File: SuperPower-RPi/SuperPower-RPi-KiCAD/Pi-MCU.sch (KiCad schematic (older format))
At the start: 30 parts, among them J5 Conn_01x06, J7 Conn_01x03, J8 Conn_01x10, J9 Conn_01x02, SW1 Tact, U3 STM32F412RETx, U4 ATtiny85-20SU, U5 ME6210A33M3G

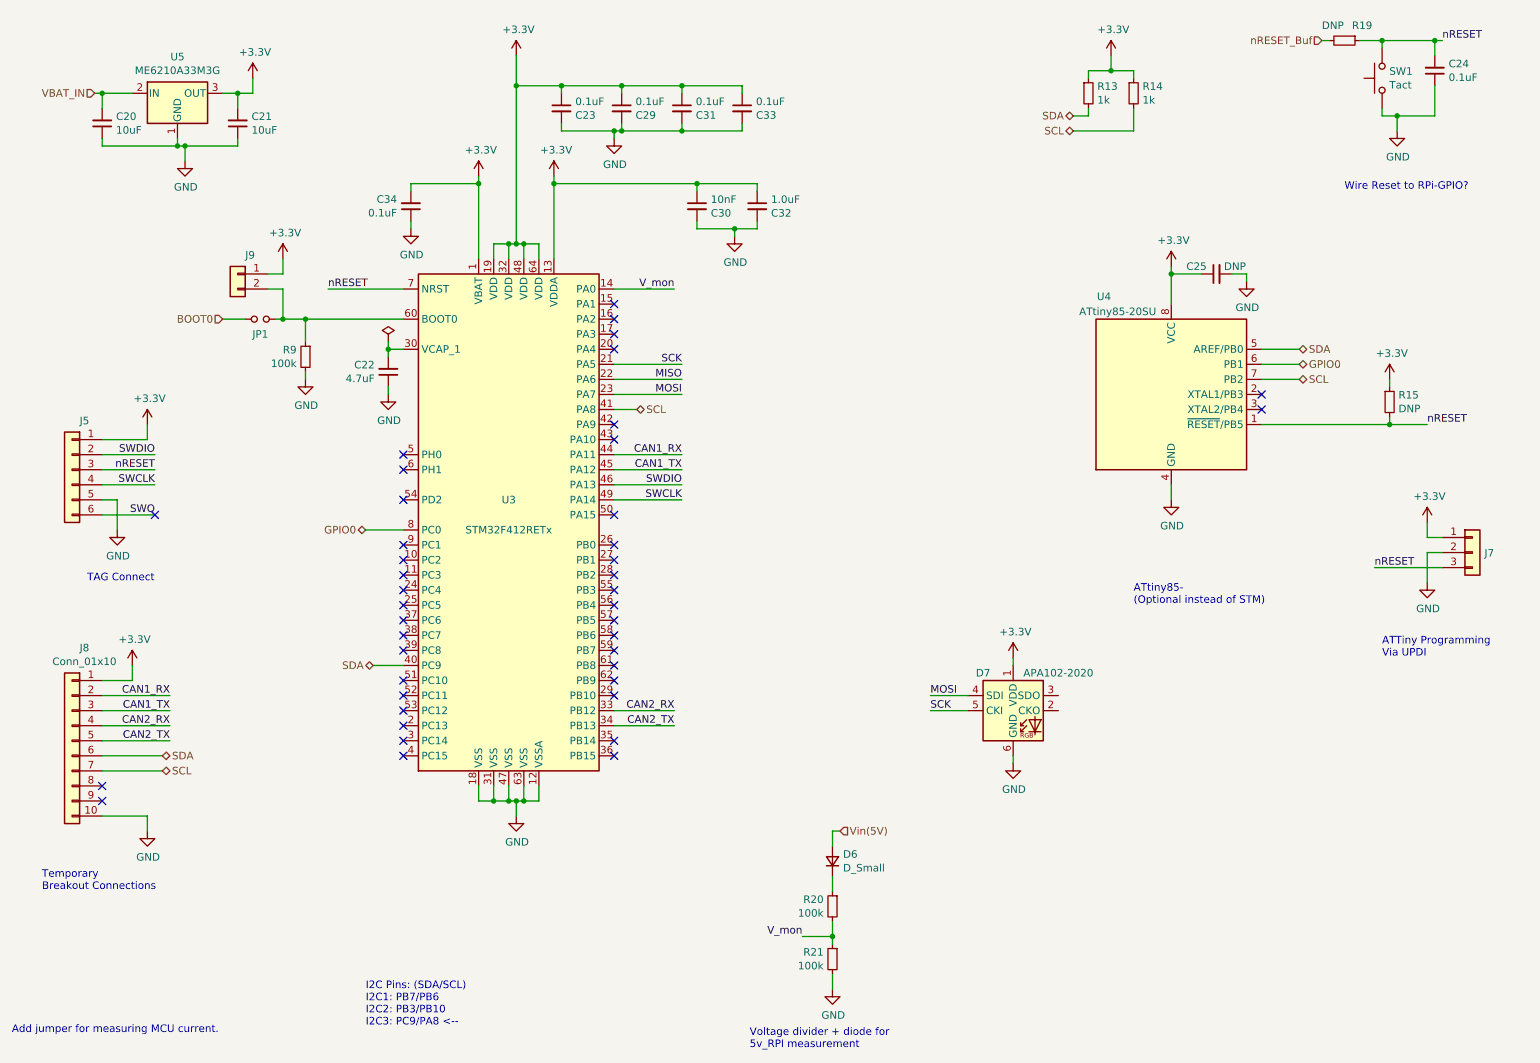
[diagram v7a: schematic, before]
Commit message: Added TODO notes from today's meeting and added some items on MCU sheet.
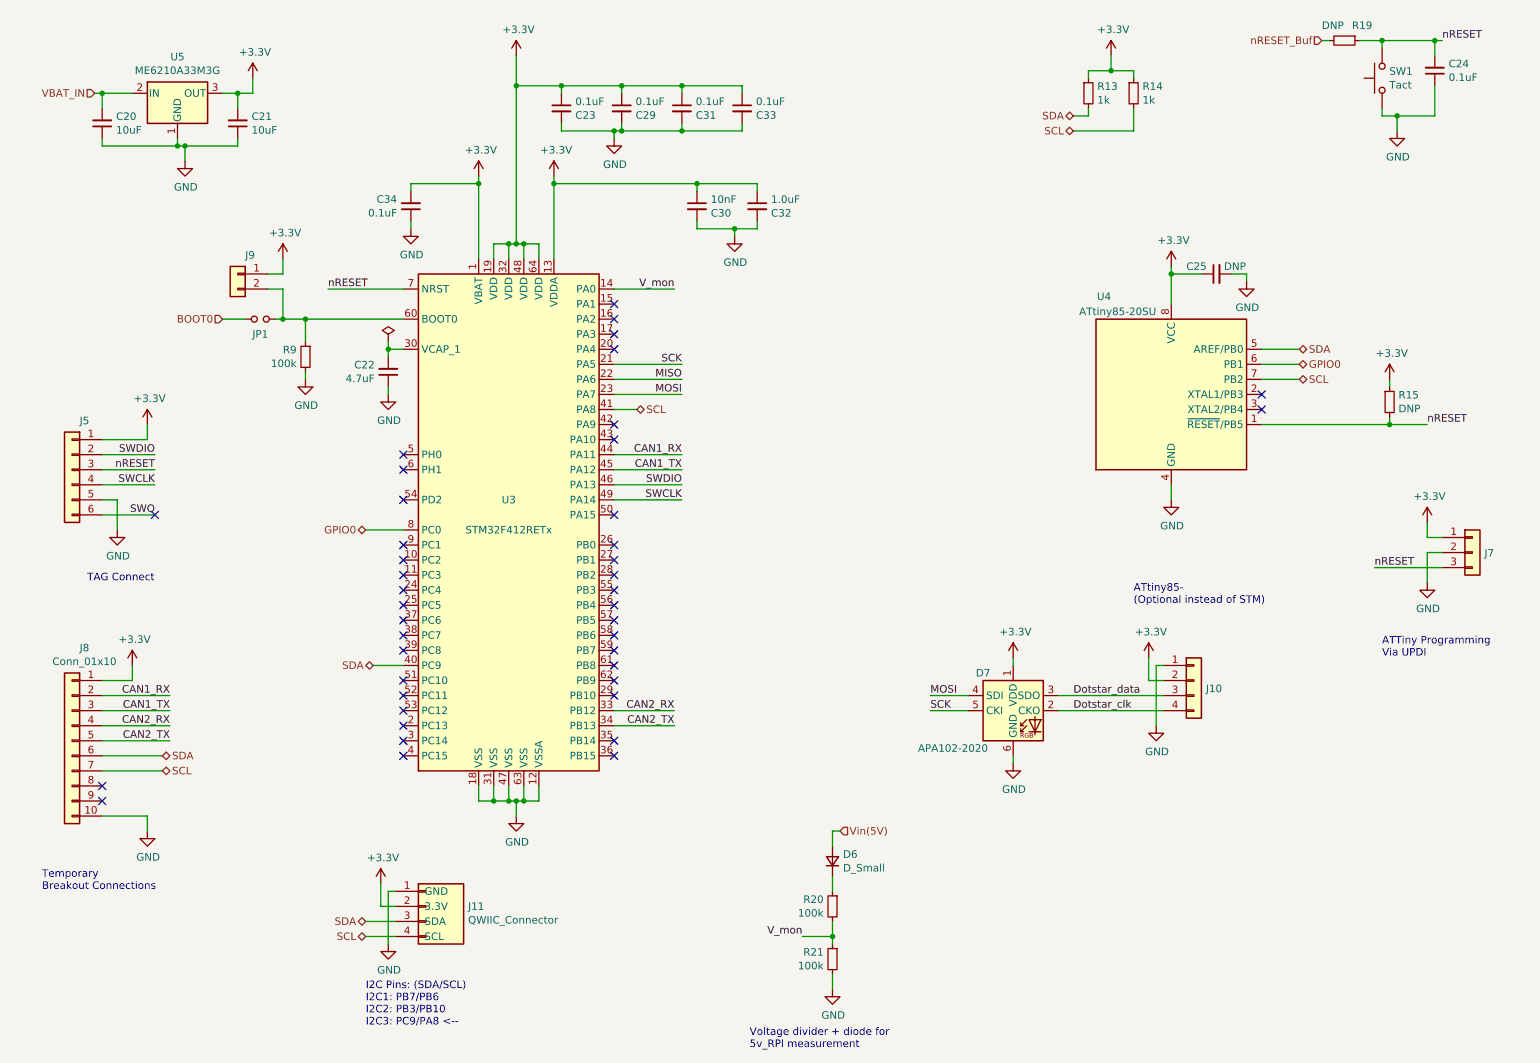
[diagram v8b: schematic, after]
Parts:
- added J10: Conn_01x04, Connector_PinHeader_2.54mm:PinHeader_1x04_P2.54mm_Vertical, symbol Connector_Generic:Conn_01x04
- added J11: QWIIC_Connector, Connector_JST:JST_SH_SM04B-SRSS-TB_1x04-1MP_P1.00mm_Horizontal, symbol !Seth_Components:QWIIC_Connector
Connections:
- net +3V3: now also J10.2 (Pin_2), J11.2 (3.3V)
- net GND: now also J10.1 (Pin_1), J11.1 (GND)
- net SCL: now also J11.4 (SCL)
- net SDA: now also J11.3 (SDA)
- net Dotstar_clk: now reaches D7.2 (CKO)
- net Dotstar_clk: now also J10.4 (Pin_4)
- net Dotstar_data: now reaches D7.3 (SDO)
- net Dotstar_data: now also J10.3 (Pin_3)
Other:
- note removed: "Add jumper for measuring MCU current."
- note removed: "Wire Reset to RPi-GPIO?"
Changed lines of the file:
@@
 $Descr A4 11693 8268
 encoding utf-8
-Sheet 8 8
+Sheet 7 8
 Title ""
 Date ""
@@
 Text HLabel 3150 4150 0    50   BiDi ~ 0
 GPIO0
-Text Notes 800  7500 0    50   ~ 0
-Add jumper for measuring MCU current.
 Text HLabel 7850 1400 0    50   BiDi ~ 0
 SDA
@@
 Wire Wire Line
 	2600 2450 2600 2350
-Text Notes 9650 1900 0    50   ~ 0
-Wire Reset to RPi-GPIO?
 $Comp
 L Device:R_Small R19
@@
 P 7450 5350
 F 0 "D7" H 7250 5600 50  0000 C CNN
-F 1 "APA102-2020" H 7750 5600 50  0000 C CNN
+F 1 "APA102-2020" H 7050 5100 50  0000 C CNN
 F 2 "LED_SMD:LED-APA102-2020" H 7500 5050 50  0001 L TNN
 F 3 "http://www.led-color.com/upload/201604/APA102-2020%20SMD%20LED.pdf" H 7550 4975 50  0001 L TNN
@@
 Wire Wire Line
 	7450 5000 7450 5050
+$Comp
+L Connector_Generic:Conn_01x04 J10
+U 1 1 5FBFB7CE
+P 8650 5150
+F 0 "J10" H 8730 5096 50  0000 L CNN
+F 1 "Conn_01x04" H 8730 5051 50  0001 L CNN
+F 2 "Connector_PinHeader_2.54mm:PinHeader_1x04_P2.54mm_Vertical" H 8650 5150 50  0001 C CNN
+F 3 "~" H 8650 5150 50  0001 C CNN
+	1    8650 5150
+	1    0    0    -1
+$EndComp
+Wire Wire Line
+	7750 5250 8450 5250
+Wire Wire Line
+	8450 5350 7750 5350
+$Comp
+L power:+3.3V #PWR042
+U 1 1 5FC175FC
+P 8350 5000
+F 0 "#PWR042" H 8350 4850 50  0001 C CNN
+F 1 "+3.3V" H 8365 5173 50  0000 C CNN
+F 2 "" H 8350 5000 50  0001 C CNN
+F 3 "" H 8350 5000 50  0001 C CNN
+	1    8350 5000
+	1    0    0    -1
+$EndComp
+Wire Wire Line
+	8450 5150 8350 5150
+Wire Wire Line
+	8350 5150 8350 5000
+$Comp
+L power:GND #PWR043
+U 1 1 5FC1F7CE
+P 8400 5450
+F 0 "#PWR043" H 8400 5200 50  0001 C CNN
+F 1 "GND" H 8405 5277 50  0000 C CNN
+F 2 "" H 8400 5450 50  0001 C CNN
+F 3 "" H 8400 5450 50  0001 C CNN
+	1    8400 5450
+	1    0    0    -1
+$EndComp
+Wire Wire Line
+	8400 5450 8400 5050
+Wire Wire Line
+	8400 5050 8450 5050
+$Comp
+L !Seth_Components:QWIIC_Connector J11
+U 1 1 5FC07762
+P 3550 6650
+F 0 "J11" H 3830 6650 50  0000 L CNN
+F 1 "QWIIC_Connector" H 3830 6559 50  0000 L CNN
+F 2 "Connector_JST:JST_SH_SM04B-SRSS-TB_1x04-1MP_P1.00mm_Horizontal" H 5200 6750 50  0001 C CNN
+F 3 "http://www.jst-mfg.com/product/pdf/eng/eSH.pdf" H 3550 6650 50  0001 C CNN
+F 4 "JST" H 3900 6600 50  0001 C CNN "Mfg"
+F 5 "SM04B-SRSS-TB(LF)(SN)" H 4300 6850 50  0001 C CNN "Mfg PN"
+F 6 "455-1804-1-ND" H 4300 6650 50  0001 C CNN "Digi-Key PN"
+	1    3550 6650
+	1    0    0    -1
+$EndComp
+Text HLabel 3150 6750 0    50   BiDi ~ 0
+SDA
+Text HLabel 3150 6850 0    50   BiDi ~ 0
+SCL
+Wire Wire Line
+	3150 6750 3350 6750
+Wire Wire Line
+	3350 6850 3150 6850
+$Comp
+L power:GND #PWR045
+U 1 1 5FC4C83C
+P 3300 6900
+F 0 "#PWR045" H 3300 6650 50  0001 C CNN
+F 1 "GND" H 3305 6727 50  0000 C CNN
+F 2 "" H 3300 6900 50  0001 C CNN
+F 3 "" H 3300 6900 50  0001 C CNN
+	1    3300 6900
+	1    0    0    -1
+$EndComp
+Wire Wire Line
+	3300 6900 3300 6550
+Wire Wire Line
+	3300 6550 3350 6550
+$Comp
+L power:+3.3V #PWR044
+U 1 1 5FC5549F
+P 3250 6500
+F 0 "#PWR044" H 3250 6350 50  0001 C CNN
+F 1 "+3.3V" H 3265 6673 50  0000 C CNN
+F 2 "" H 3250 6500 50  0001 C CNN
+F 3 "" H 3250 6500 50  0001 C CNN
+	1    3250 6500
+	1    0    0    -1
+$EndComp
+Wire Wire Line
+	3250 6500 3250 6650
+Wire Wire Line
+	3250 6650 3350 6650
+Text Label 7850 5250 0    50   ~ 0
+Dotstar_data
+Text Label 7850 5350 0    50   ~ 0
+Dotstar_clk
 $EndSCHEMATC
